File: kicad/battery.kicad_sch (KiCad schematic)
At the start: 6 parts

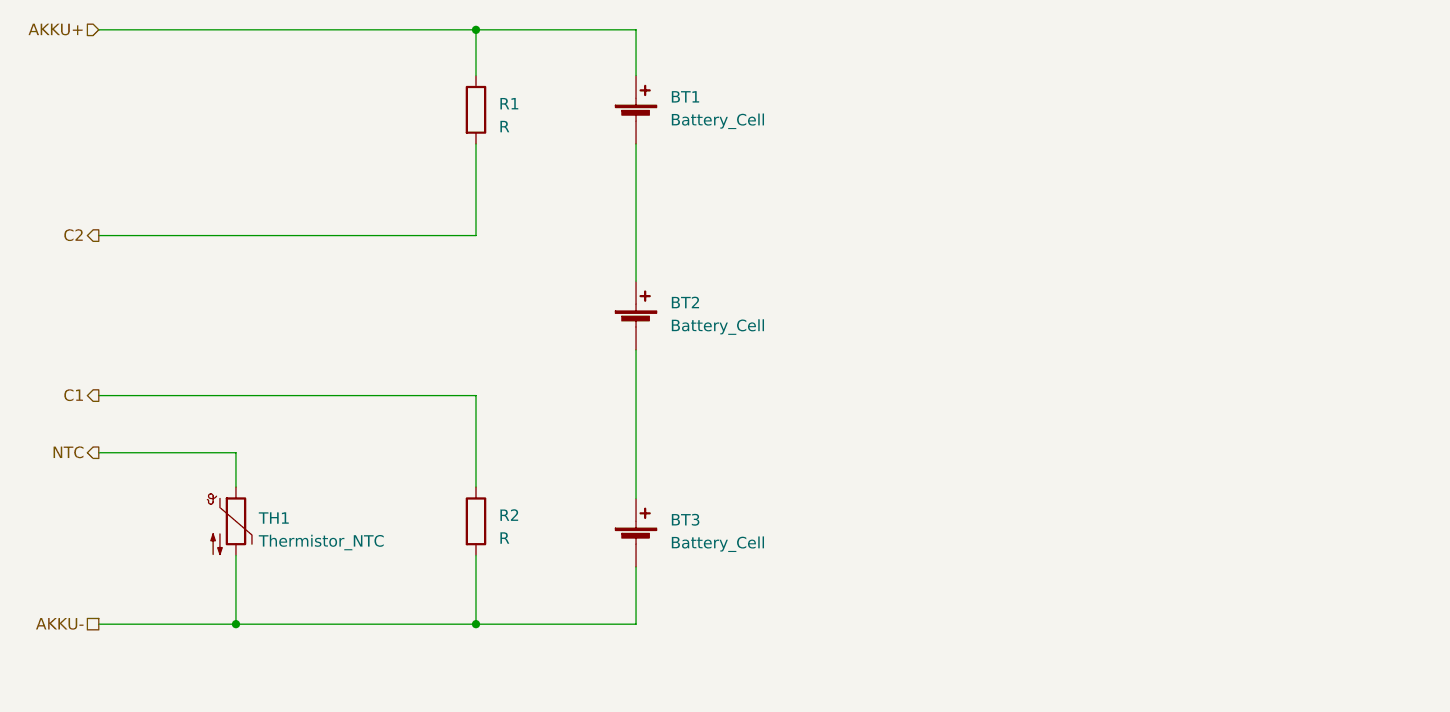
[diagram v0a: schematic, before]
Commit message: Update README.md and battery schematic
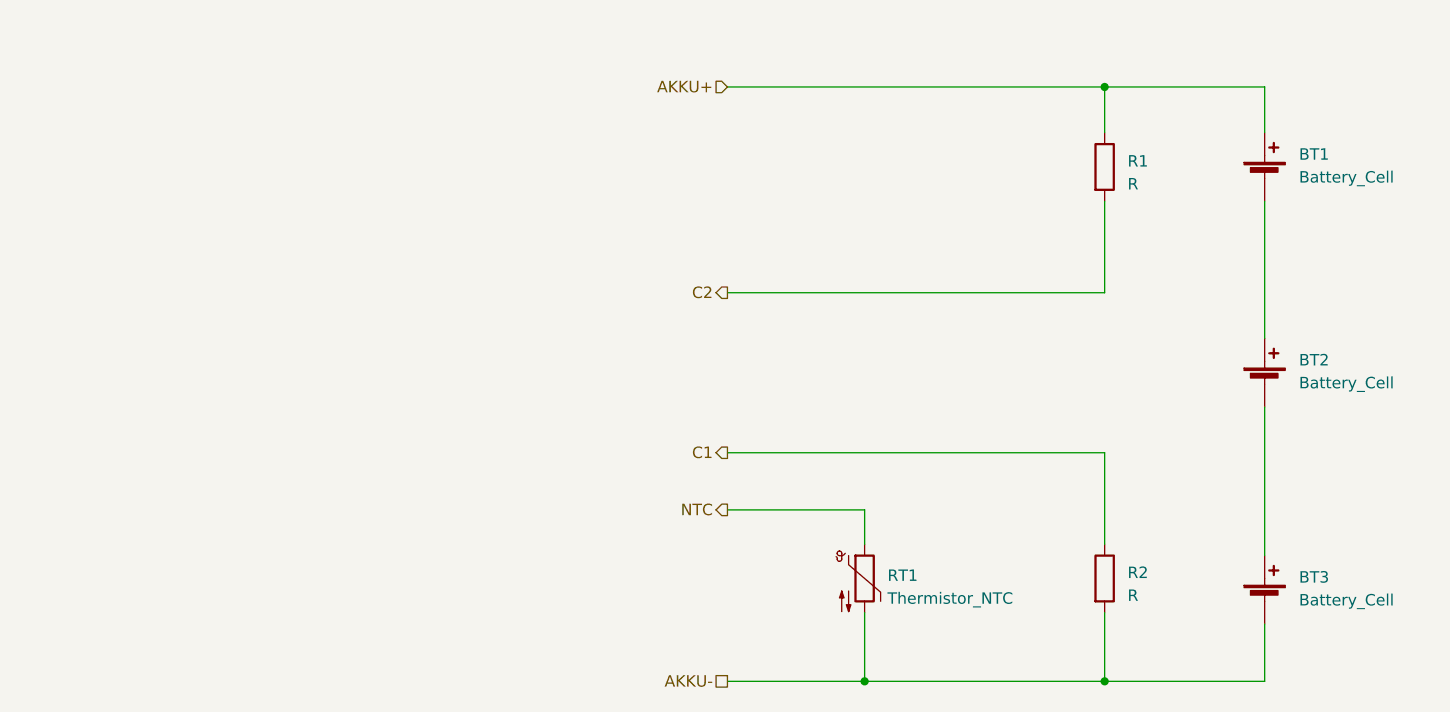
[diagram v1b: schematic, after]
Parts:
- renumbered TH1 to RT1
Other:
- moved on the sheet: BT1, BT2, BT3, R1, R2, RT1

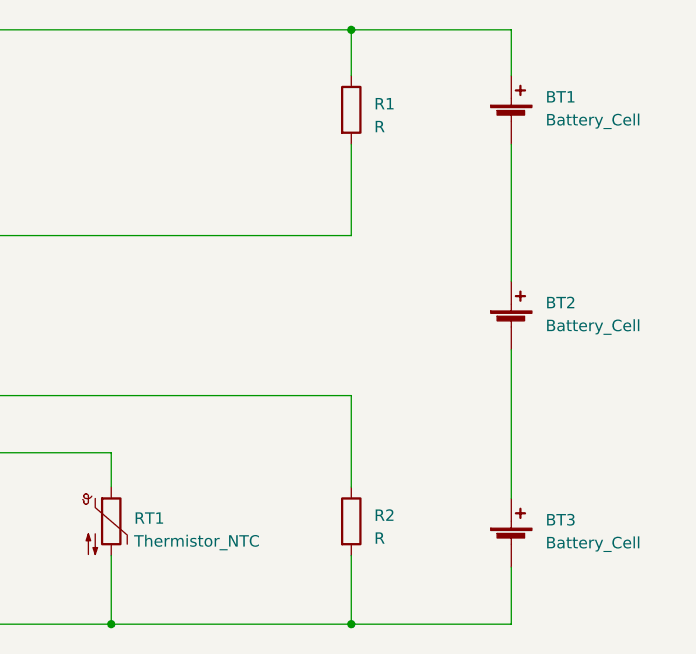
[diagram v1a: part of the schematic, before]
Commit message: Add footprints
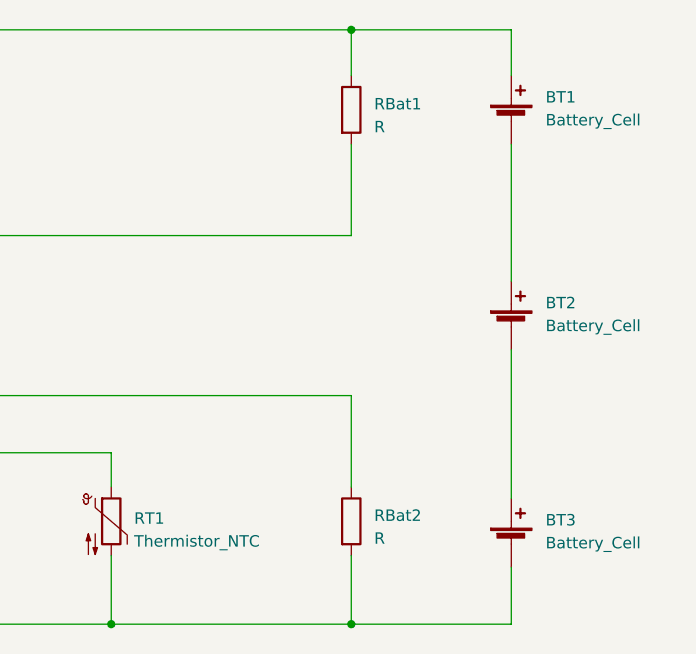
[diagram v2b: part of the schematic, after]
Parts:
- RBat1: renamed from R1; footprint (none) -> Resistor_THT:R_Axial_DIN0207_L6.3mm_D2.5mm_P10.16mm_Horizontal
- RBat2: renamed from R2; footprint (none) -> Resistor_THT:R_Axial_DIN0207_L6.3mm_D2.5mm_P10.16mm_Horizontal
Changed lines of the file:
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@@
   )
   (symbol (lib_id "Device:Battery_Cell") (at 177.8 68.58 0) (unit 1)
-    (in_bom yes) (on_board yes) (dnp no) (fields_autoplaced)
+    (in_bom yes) (on_board no) (dnp no) (fields_autoplaced)
     (property "Reference" "BT1" (at 181.61 65.913 0)
       (effects (font (size 1.27 1.27)) (justify left))
@@
   )
   (symbol (lib_id "Device:R") (at 160.02 113.03 0) (unit 1)
-    (in_bom yes) (on_board yes) (dnp no) (fields_autoplaced)
-    (property "Reference" "R2" (at 162.56 112.395 0)
+    (in_bom yes) (on_board no) (dnp no) (fields_autoplaced)
+    (property "Reference" "RBat2" (at 162.56 112.395 0)
       (effects (font (size 1.27 1.27)) (justify left))
     )
@@
       (effects (font (size 1.27 1.27)) (justify left))
     )
-    (property "Footprint" "" (at 158.242 113.03 90)
+    (property "Footprint" "Resistor_THT:R_Axial_DIN0207_L6.3mm_D2.5mm_P10.16mm_Horizontal" (at 158.242 113.03 90)
       (effects (font (size 1.27 1.27)) hide)
     )
@@
       (project "Dremel_PCB1857_V1"
         (path "/ab18b4c8-6f40-44db-bccd-b69c22b3ada9/5fd66d92-b6c6-4b69-8334-9a644953f52a"
-          (reference "R2") (unit 1)
+          (reference "RBat2") (unit 1)
         )
       )
@@
   )
   (symbol (lib_id "Device:Battery_Cell") (at 177.8 91.44 0) (unit 1)
-    (in_bom yes) (on_board yes) (dnp no) (fields_autoplaced)
+    (in_bom yes) (on_board no) (dnp no) (fields_autoplaced)
     (property "Reference" "BT2" (at 181.61 88.773 0)
       (effects (font (size 1.27 1.27)) (justify left))
@@
   )
   (symbol (lib_id "Device:Battery_Cell") (at 177.8 115.57 0) (unit 1)
-    (in_bom yes) (on_board yes) (dnp no) (fields_autoplaced)
+    (in_bom yes) (on_board no) (dnp no) (fields_autoplaced)
     (property "Reference" "BT3" (at 181.61 112.903 0)
       (effects (font (size 1.27 1.27)) (justify left))
@@
   )
   (symbol (lib_id "Device:R") (at 160.02 67.31 0) (unit 1)
-    (in_bom yes) (on_board yes) (dnp no) (fields_autoplaced)
-    (property "Reference" "R1" (at 162.56 66.675 0)
+    (in_bom yes) (on_board no) (dnp no) (fields_autoplaced)
+    (property "Reference" "RBat1" (at 162.56 66.675 0)
       (effects (font (size 1.27 1.27)) (justify left))
     )
@@
       (effects (font (size 1.27 1.27)) (justify left))
     )
-    (property "Footprint" "" (at 158.242 67.31 90)
+    (property "Footprint" "Resistor_THT:R_Axial_DIN0207_L6.3mm_D2.5mm_P10.16mm_Horizontal" (at 158.242 67.31 90)
       (effects (font (size 1.27 1.27)) hide)
     )
@@
       (project "Dremel_PCB1857_V1"
         (path "/ab18b4c8-6f40-44db-bccd-b69c22b3ada9/5fd66d92-b6c6-4b69-8334-9a644953f52a"
-          (reference "R1") (unit 1)
+          (reference "RBat1") (unit 1)
         )
       )
@@
   )
   (symbol (lib_id "Device:Thermistor_NTC") (at 133.35 113.03 0) (unit 1)
-    (in_bom yes) (on_board yes) (dnp no) (fields_autoplaced)
+    (in_bom yes) (on_board no) (dnp no) (fields_autoplaced)
     (property "Reference" "RT1" (at 135.89 112.7125 0)
       (effects (font (size 1.27 1.27)) (justify left))
